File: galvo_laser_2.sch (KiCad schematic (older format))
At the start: 22 parts, among them J1 Conn_01x01_Female, J2 Conn_01x01_Female, J3 Conn_01x03_Male, J4 Conn_01x03_Male, J5 AudioJack3, J6 Screw_Terminal_01x01, U1 LM324D

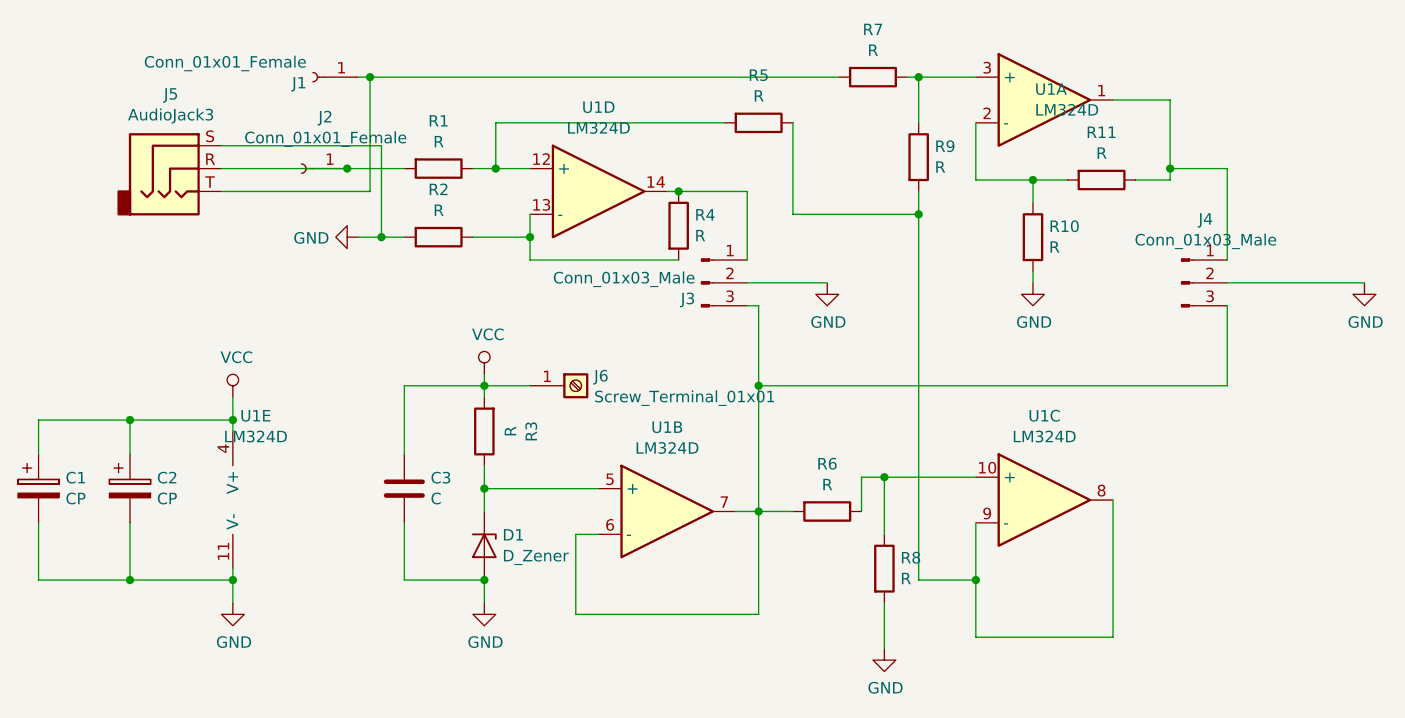
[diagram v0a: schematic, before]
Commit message: Add resistor values
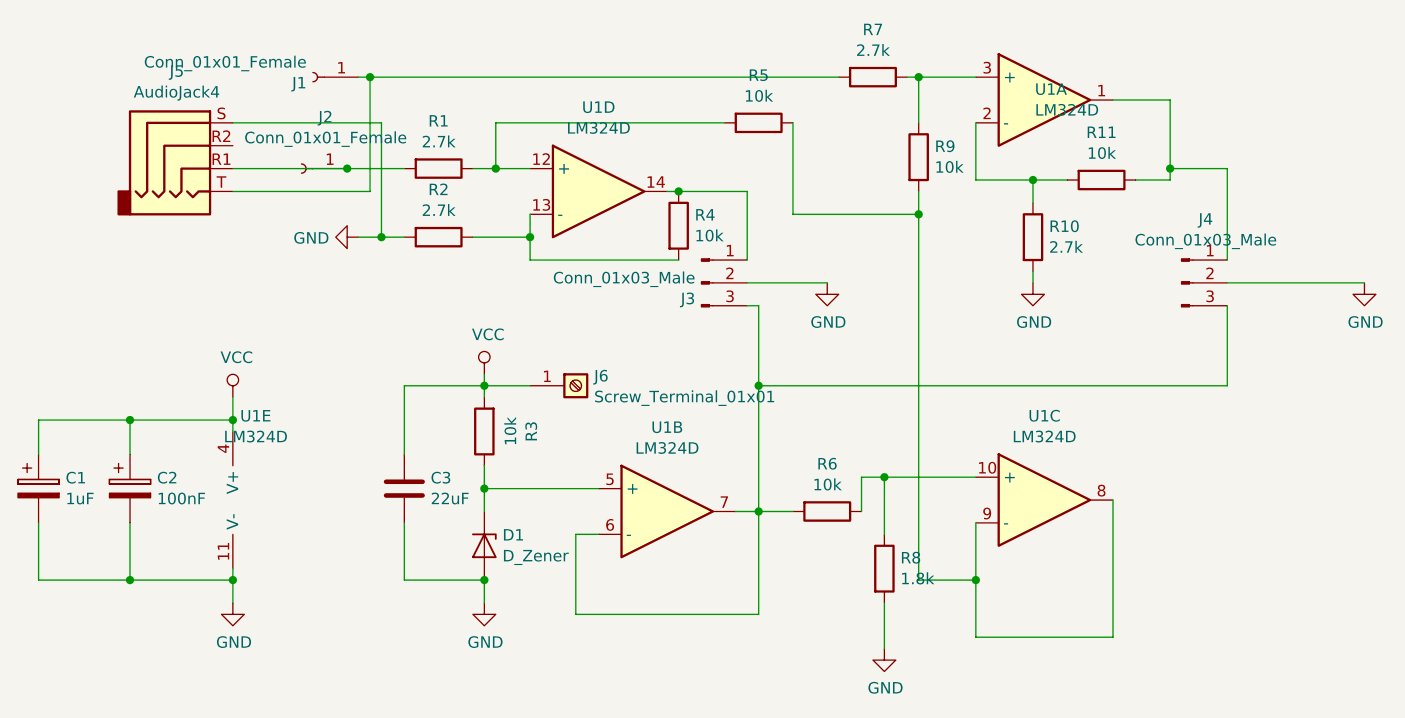
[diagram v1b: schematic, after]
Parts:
- removed J5: AudioJack3, Connector_Audio:Jack_3.5mm_CUI_SJ1-3533NG_Horizontal, symbol Connector:AudioJack3
- added J5: AudioJack4, Connector_Audio:Jack_3.5mm_PJ320D_Horizontal, symbol Connector:AudioJack4
- C1: value CP -> 1uF
- C2: value CP -> 100nF
- C3: value C -> 22uF
- R1, R10, R2, R7: value R -> 2.7k
- R11, R3, R4, R5, R6, R9: value R -> 10k
- R8: value R -> 1.8k
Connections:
- net GND: now also J5.S
- net at J1.1 (Pin_1), R7.2: now also J5.T
- net at J2.1 (Pin_1), R1.2: now also J5.R1
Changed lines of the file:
@@
 P 6900 2700
 F 0 "R10" H 6970 2746 50  0000 L CNN
-F 1 "R" H 6970 2655 50  0000 L CNN
+F 1 "2.7k" H 6970 2655 50  0000 L CNN
 F 2 "Resistor_SMD:R_0603_1608Metric" V 6830 2700 50  0001 C CNN
 F 3 "~" H 6900 2700 50  0001 C CNN
@@
 P 7200 2450
 F 0 "R11" V 6993 2450 50  0000 C CNN
-F 1 "R" V 7084 2450 50  0000 C CNN
+F 1 "10k" V 7084 2450 50  0000 C CNN
 F 2 "Resistor_SMD:R_0603_1608Metric" V 7130 2450 50  0001 C CNN
 F 3 "~" H 7200 2450 50  0001 C CNN
@@
 P 6200 2000
 F 0 "R7" V 5993 2000 50  0000 C CNN
-F 1 "R" V 6084 2000 50  0000 C CNN
+F 1 "2.7k" V 6084 2000 50  0000 C CNN
 F 2 "Resistor_SMD:R_0603_1608Metric" V 6130 2000 50  0001 C CNN
 F 3 "~" H 6200 2000 50  0001 C CNN
@@
 P 6400 2350
 F 0 "R9" H 6470 2396 50  0000 L CNN
-F 1 "R" H 6470 2305 50  0000 L CNN
+F 1 "10k" H 6470 2305 50  0000 L CNN
 F 2 "Resistor_SMD:R_0603_1608Metric" V 6330 2350 50  0001 C CNN
 F 3 "~" H 6400 2350 50  0001 C CNN
@@
 P 6000 3900
 F 0 "R6" V 5793 3900 50  0000 C CNN
-F 1 "R" V 5884 3900 50  0000 C CNN
+F 1 "10k" V 5884 3900 50  0000 C CNN
 F 2 "Resistor_SMD:R_0603_1608Metric" V 5930 3900 50  0001 C CNN
 F 3 "~" H 6000 3900 50  0001 C CNN
@@
 P 6250 4150
 F 0 "R8" H 6320 4196 50  0000 L CNN
-F 1 "R" H 6320 4105 50  0000 L CNN
+F 1 "1.8k" H 6320 4105 50  0000 L CNN
 F 2 "Resistor_SMD:R_0603_1608Metric" V 6180 4150 50  0001 C CNN
 F 3 "~" H 6250 4150 50  0001 C CNN
@@
 P 4500 3550
 F 0 "R3" V 4293 3550 50  0000 C CNN
-F 1 "R" V 4384 3550 50  0000 C CNN
+F 1 "10k" V 4384 3550 50  0000 C CNN
 F 2 "Resistor_SMD:R_0603_1608Metric" V 4430 3550 50  0001 C CNN
 F 3 "~" H 4500 3550 50  0001 C CNN
@@
 P 5350 2650
 F 0 "R4" H 5420 2696 50  0000 L CNN
-F 1 "R" H 5420 2605 50  0000 L CNN
+F 1 "10k" H 5420 2605 50  0000 L CNN
 F 2 "Resistor_SMD:R_0603_1608Metric" V 5280 2650 50  0001 C CNN
 F 3 "~" H 5350 2650 50  0001 C CNN
@@
 P 4300 2700
 F 0 "R2" V 4093 2700 50  0000 C CNN
-F 1 "R" V 4184 2700 50  0000 C CNN
+F 1 "2.7k" V 4184 2700 50  0000 C CNN
 F 2 "Resistor_SMD:R_0603_1608Metric" V 4230 2700 50  0001 C CNN
 F 3 "~" H 4300 2700 50  0001 C CNN
@@
 P 5700 2200
 F 0 "R5" V 5493 2200 50  0000 C CNN
-F 1 "R" V 5584 2200 50  0000 C CNN
+F 1 "10k" V 5584 2200 50  0000 C CNN
 F 2 "Resistor_SMD:R_0603_1608Metric" V 5630 2200 50  0001 C CNN
 F 3 "~" H 5700 2200 50  0001 C CNN
@@
 P 4300 2400
 F 0 "R1" V 4093 2400 50  0000 C CNN
-F 1 "R" V 4184 2400 50  0000 C CNN
+F 1 "2.7k" V 4184 2400 50  0000 C CNN
 F 2 "Resistor_SMD:R_0603_1608Metric" V 4230 2400 50  0001 C CNN
 F 3 "~" H 4300 2400 50  0001 C CNN
@@
 Wire Wire Line
 	3400 4300 3400 4200
-$Comp
-L Connector:AudioJack3 J5
-U 1 1 5C64E839
-P 3150 2400
-F 0 "J5" H 3130 2725 50  0000 C CNN
-F 1 "AudioJack3" H 3130 2634 50  0000 C CNN
-F 2 "Connector_Audio:Jack_3.5mm_CUI_SJ1-3533NG_Horizontal" H 3150 2400 50  0001 C CNN
-F 3 "~" H 3150 2400 50  0001 C CNN
-	1    3150 2400
-	1    0    0    -1
-$EndComp
-Wire Wire Line
-	3350 2300 4050 2300
-Wire Wire Line
-	4050 2300 4050 2700
 Connection ~ 4050 2700
 Wire Wire Line
 	4050 2700 4150 2700
 Wire Wire Line
-	3350 2400 3900 2400
-Connection ~ 3900 2400
-Wire Wire Line
 	3900 2400 4150 2400
 Wire Wire Line
 	3950 2000 4000 2000
-Wire Wire Line
-	3350 2500 4000 2500
 Wire Wire Line
 	4000 2500 4000 2000
@@
 P 4150 3800
 F 0 "C3" H 4265 3846 50  0000 L CNN
-F 1 "C" H 4265 3755 50  0000 L CNN
+F 1 "22uF" H 4265 3755 50  0000 L CNN
 F 2 "Capacitor_Tantalum_SMD:CP_EIA-3216-18_Kemet-A" H 4188 3650 50  0001 C CNN
 F 3 "~" H 4150 3800 50  0001 C CNN
@@
 P 2950 3800
 F 0 "C2" H 3068 3846 50  0000 L CNN
-F 1 "CP" H 3068 3755 50  0000 L CNN
+F 1 "100nF" H 3068 3755 50  0000 L CNN
 F 2 "Capacitor_SMD:C_0805_2012Metric" H 2988 3650 50  0001 C CNN
 F 3 "~" H 2950 3800 50  0001 C CNN
@@
 P 2550 3800
 F 0 "C1" H 2668 3846 50  0000 L CNN
-F 1 "CP" H 2668 3755 50  0000 L CNN
+F 1 "1uF" H 2668 3755 50  0000 L CNN
 F 2 "Capacitor_SMD:C_0603_1608Metric" H 2588 3650 50  0001 C CNN
 F 3 "~" H 2550 3800 50  0001 C CNN
@@
 Wire Wire Line
 	4700 3350 4500 3350
+$Comp
+L Connector:AudioJack4 J5
+U 1 1 5C8D5147
+P 3200 2300
+F 0 "J5" H 3155 2625 50  0000 C CNN
+F 1 "AudioJack4" H 3155 2534 50  0000 C CNN
+F 2 "Connector_Audio:Jack_3.5mm_PJ320D_Horizontal" H 3200 2300 50  0001 C CNN
+F 3 "~" H 3200 2300 50  0001 C CNN
+	1    3200 2300
+	1    0    0    -1
+$EndComp
+Wire Wire Line
+	3400 2200 4050 2200
+Wire Wire Line
+	4050 2200 4050 2700
+Wire Wire Line
+	3400 2500 4000 2500
+Wire Wire Line
+	3400 2400 3900 2400
+Connection ~ 3900 2400
 $EndSCHEMATC

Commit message: Connect screw terminal to ground
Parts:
- removed J6: Screw_Terminal_01x01, TerminalBlock_Phoenix:TerminalBlock_Phoenix_MKDS-1,5-2_1x02_P5.00mm_Horizontal, symbol Connector:Screw_Terminal_01x01
- added J6: Screw_Terminal_01x02, TerminalBlock_Phoenix:TerminalBlock_Phoenix_MKDS-1,5-2_1x02_P5.00mm_Horizontal, symbol Connector:Screw_Terminal_01x02
- C1, C2: symbol Device:CP -> Device:C
- C3: symbol Device:C -> Device:CP
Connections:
- net GND: now also J6.2 (Pin_2)
- net VCC: now also J6.1 (Pin_1)
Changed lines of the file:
@@
 	4000 2000 6050 2000
 $Comp
-L Device:C C3
+L Device:CP C3
 U 1 1 5C63A231
 P 4150 3800
@@
 Connection ~ 4500 4200
 $Comp
-L Device:CP C2
+L Device:C C2
 U 1 1 5C63FB9A
 P 2950 3800
@@
 $EndComp
 $Comp
-L Device:CP C1
+L Device:C C1
 U 1 1 5C63FC20
 P 2550 3800
@@
 Wire Wire Line
 	2950 4200 2550 4200
-$Comp
-L Connector:Screw_Terminal_01x01 J6
-U 1 1 5C64BD3F
-P 4900 3350
-F 0 "J6" H 4980 3392 50  0000 L CNN
-F 1 "Screw_Terminal_01x01" H 4980 3301 50  0000 L CNN
-F 2 "TerminalBlock_Phoenix:TerminalBlock_Phoenix_MKDS-1,5-2_1x02_P5.00mm_Horizontal" H 4900 3350 50  0001 C CNN
-F 3 "~" H 4900 3350 50  0001 C CNN
-	1    4900 3350
-	1    0    0    -1
-$EndComp
 Wire Wire Line
 	3400 3400 3400 3500
-Wire Wire Line
-	4700 3350 4500 3350
 $Comp
 L Connector:AudioJack4 J5
@@
 	3400 2400 3900 2400
 Connection ~ 3900 2400
+$Comp
+L Connector:Screw_Terminal_01x02 J6
+U 1 1 5CA28408
+P 4900 3100
+F 0 "J6" H 4980 3092 50  0000 L CNN
+F 1 "Screw_Terminal_01x02" H 4980 3001 50  0000 L CNN
+F 2 "TerminalBlock_Phoenix:TerminalBlock_Phoenix_MKDS-1,5-2_1x02_P5.00mm_Horizontal" H 4900 3100 50  0001 C CNN
+F 3 "~" H 4900 3100 50  0001 C CNN
+	1    4900 3100
+	1    0    0    -1
+$EndComp
+Wire Wire Line
+	4700 3100 4600 3100
+Wire Wire Line
+	4600 3100 4600 3350
+Wire Wire Line
+	4600 3350 4500 3350
+Wire Wire Line
+	4700 3200 4700 4300
+Wire Wire Line
+	4700 4300 4500 4300
+Connection ~ 4500 4300
 $EndSCHEMATC

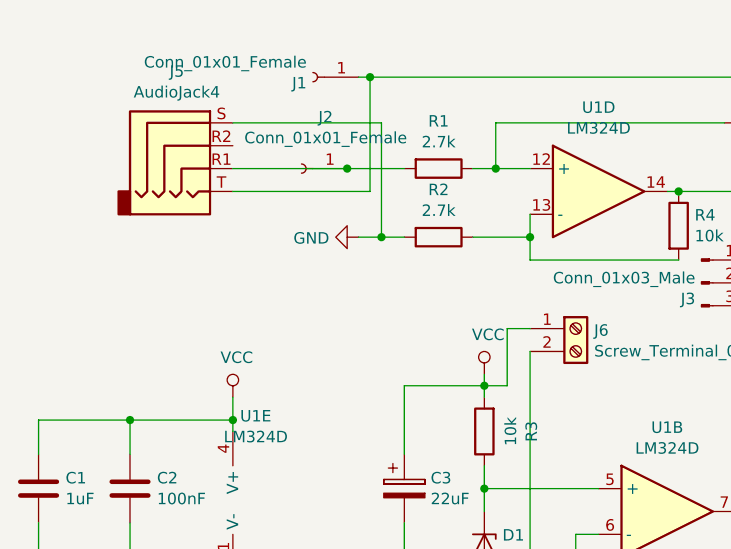
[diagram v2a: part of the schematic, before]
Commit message: Add ground connector for microcontroller
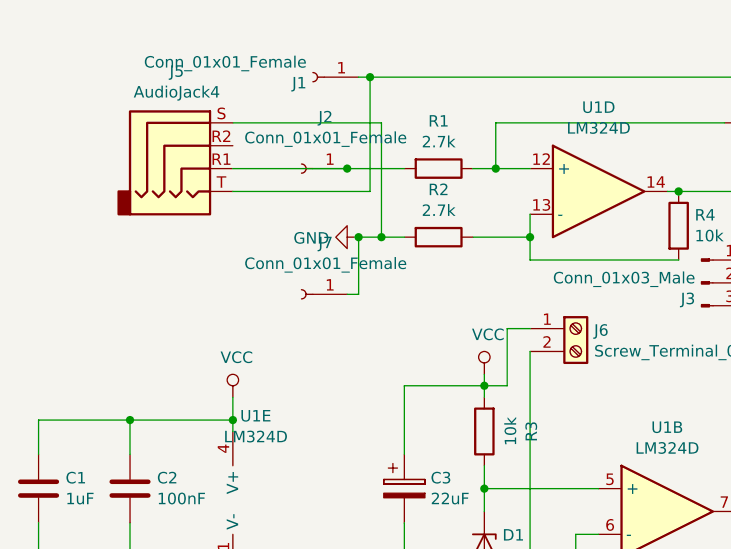
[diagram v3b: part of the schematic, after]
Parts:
- added J7: Conn_01x01_Female, Connector_PinHeader_2.54mm:PinHeader_1x01_P2.54mm_Vertical, symbol Connector:Conn_01x01_Female
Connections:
- net GND: now also J7.1 (Pin_1)
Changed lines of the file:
@@
 	4700 4300 4500 4300
 Connection ~ 4500 4300
+$Comp
+L Connector:Conn_01x01_Female J7
+U 1 1 5CA3AED7
+P 3700 2950
+F 0 "J7" H 3594 2725 50  0000 C CNN
+F 1 "Conn_01x01_Female" H 3594 2816 50  0000 C CNN
+F 2 "Connector_PinHeader_2.54mm:PinHeader_1x01_P2.54mm_Vertical" H 3700 2950 50  0001 C CNN
+F 3 "~" H 3700 2950 50  0001 C CNN
+	1    3700 2950
+	-1   0    0    1
+$EndComp
+Wire Wire Line
+	3900 2950 3950 2950
+Wire Wire Line
+	3950 2950 3950 2700
+Connection ~ 3950 2700
 $EndSCHEMATC
